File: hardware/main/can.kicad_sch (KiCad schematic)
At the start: 9 parts

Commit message: Schematics: finalize Analog Snubber and Supplies
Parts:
- C701: value ~ -> 50V 100nF X7R ±10% 0402
- C702: value ~ -> 50V 4.7n
- D701: renamed from D201; value ~ -> PESD1CAN
- R701: value ~ -> 4k7
- R702: value ~ -> 300R
- R703, R704: value ~ -> 520R
- R705: renamed from R202; value ~ -> NC
- renumbered U201 to U701
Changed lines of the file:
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@@
   (symbol (lib_id "power:GND") (at 133.35 101.6 0) (unit 1)
     (in_bom yes) (on_board yes)
-    (property "Reference" "#PWR0184" (id 0) (at 133.35 107.95 0)
+    (property "Reference" "#PWR0702" (id 0) (at 133.35 107.95 0)
       (effects (font (size 1.27 1.27)) hide)
     )
@@
       (effects (font (size 1.27 1.27)) (justify left))
     )
-    (property "Value" "~" (id 1) (at 117.0686 98.933 0)
+    (property "Value" "4k7" (id 1) (at 117.0686 98.933 0)
       (effects (font (size 1.27 1.27)) (justify left))
     )
@@
   (symbol (lib_id "power:GND") (at 118.11 76.2 0) (unit 1)
     (in_bom yes) (on_board yes)
-    (property "Reference" "#PWR0183" (id 0) (at 118.11 82.55 0)
+    (property "Reference" "#PWR0701" (id 0) (at 118.11 82.55 0)
       (effects (font (size 1.27 1.27)) hide)
     )
@@
     (in_bom yes) (on_board yes)
     (property "Reference" "C701" (id 0) (at 125.73 70.3834 90))
-    (property "Value" "~" (id 1) (at 125.73 72.6948 90))
+    (property "Value" "50V 100nF X7R ±10% 0402" (id 1) (at 125.73 72.6948 90))
     (property "Footprint" "" (id 2) (at 125.73 76.2 0)
       (effects (font (size 1.27 1.27)) hide)
     )
-    (property "Datasheet" "~" (id 3) (at 125.73 76.2 0)
+    (property "Datasheet" "https://lcsc.com/product-detail/Multilayer-Ceramic-Capacitors-MLCC-SMD-SMT_Murata-Electronics-GRM155R71H104KE14D_C77020.html" (id 3) (at 125.73 76.2 0)
       (effects (font (size 1.27 1.27)) hide)
     )
@@
   (symbol (lib_id "Interface_CAN_LIN:MCP2561-E-SN") (at 133.35 87.63 0) (unit 1)
     (in_bom yes) (on_board yes)
-    (property "Reference" "U201" (id 0) (at 133.35 72.8726 0))
+    (property "Reference" "U701" (id 0) (at 133.35 72.8726 0))
     (property "Value" "~" (id 1) (at 133.35 75.184 0))
     (property "Footprint" "" (id 2) (at 133.35 100.33 0)
@@
   (symbol (lib_id "Controle-rescue:D_TVS_x2_AAC-Device") (at 179.07 110.49 0) (unit 1)
     (in_bom yes) (on_board yes)
-    (property "Reference" "D201" (id 0) (at 179.07 104.9782 0))
-    (property "Value" "~" (id 1) (at 179.07 107.2896 0))
+    (property "Reference" "D701" (id 0) (at 179.07 104.9782 0))
+    (property "Value" "PESD1CAN" (id 1) (at 179.07 107.2896 0))
     (property "Footprint" "" (id 2) (at 179.07 110.49 0)
       (effects (font (size 1.27 1.27)) hide)
@@
   (symbol (lib_id "Device:R_Small") (at 179.07 102.87 270) (unit 1)
     (in_bom yes) (on_board yes)
-    (property "Reference" "R202" (id 0) (at 179.07 97.8916 90))
-    (property "Value" "~" (id 1) (at 179.07 100.203 90))
+    (property "Reference" "R705" (id 0) (at 179.07 97.8916 90))
+    (property "Value" "NC" (id 1) (at 179.07 100.203 90))
     (property "Footprint" "" (id 2) (at 179.07 102.87 0)
       (effects (font (size 1.27 1.27)) hide)
@@
   (symbol (lib_id "power:GND") (at 179.07 116.84 0) (unit 1)
     (in_bom yes) (on_board yes)
-    (property "Reference" "#PWR0182" (id 0) (at 179.07 123.19 0)
+    (property "Reference" "#PWR0704" (id 0) (at 179.07 123.19 0)
       (effects (font (size 1.27 1.27)) hide)
     )
@@
       (effects (font (size 1.27 1.27)) (justify left))
     )
-    (property "Value" "~" (id 1) (at 151.257 89.1286 0)
+    (property "Value" "300R" (id 1) (at 151.257 89.1286 0)
       (effects (font (size 1.27 1.27)) (justify left))
     )
@@
       (effects (font (size 1.27 1.27)) (justify left))
     )
-    (property "Value" "~" (id 1) (at 158.9786 81.407 0)
+    (property "Value" "520R" (id 1) (at 158.9786 81.407 0)
       (effects (font (size 1.27 1.27)) (justify left))
     )
@@
       (effects (font (size 1.27 1.27)) (justify left))
     )
-    (property "Value" "~" (id 1) (at 158.9786 91.567 0)
+    (property "Value" "520R" (id 1) (at 158.9786 91.567 0)
       (effects (font (size 1.27 1.27)) (justify left))
     )
@@
     (in_bom yes) (on_board yes)
     (property "Reference" "C702" (id 0) (at 167.64 81.8134 90))
-    (property "Value" "~" (id 1) (at 167.64 84.1248 90))
+    (property "Value" "50V 4.7n " (id 1) (at 167.64 84.1248 90))
     (property "Footprint" "" (id 2) (at 167.64 87.63 0)
       (effects (font (size 1.27 1.27)) hide)
@@
   (symbol (lib_id "power:GND") (at 175.26 88.9 0) (unit 1)
     (in_bom yes) (on_board yes)
-    (property "Reference" "#PWR0181" (id 0) (at 175.26 95.25 0)
+    (property "Reference" "#PWR0703" (id 0) (at 175.26 95.25 0)
       (effects (font (size 1.27 1.27)) hide)
     )

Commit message: Schematics: Modified component values
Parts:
- C702: value 50V 4.7n -> 50V 4.7nF X7R ±5% 0603
- R701: value 4k7 -> 4k7 0805
- R702: value 300R -> 300R 0805
- R703, R704: value 520R -> 520R 0805
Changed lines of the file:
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@@
       (effects (font (size 1.27 1.27)) (justify left))
     )
-    (property "Value" "4k7" (id 1) (at 117.0686 98.933 0)
+    (property "Value" "4k7 0805" (id 1) (at 117.0686 98.933 0)
       (effects (font (size 1.27 1.27)) (justify left))
     )
@@
       (effects (font (size 1.27 1.27)) (justify left))
     )
-    (property "Value" "300R" (id 1) (at 151.257 89.1286 0)
+    (property "Value" "300R 0805" (id 1) (at 151.257 89.1286 0)
       (effects (font (size 1.27 1.27)) (justify left))
     )
@@
       (effects (font (size 1.27 1.27)) (justify left))
     )
-    (property "Value" "520R" (id 1) (at 158.9786 81.407 0)
+    (property "Value" "520R 0805" (id 1) (at 158.9786 81.407 0)
       (effects (font (size 1.27 1.27)) (justify left))
     )
@@
       (effects (font (size 1.27 1.27)) (justify left))
     )
-    (property "Value" "520R" (id 1) (at 158.9786 91.567 0)
+    (property "Value" "520R 0805" (id 1) (at 158.9786 91.567 0)
       (effects (font (size 1.27 1.27)) (justify left))
     )
@@
     (in_bom yes) (on_board yes)
     (property "Reference" "C702" (id 0) (at 167.64 81.8134 90))
-    (property "Value" "50V 4.7n " (id 1) (at 167.64 84.1248 90))
+    (property "Value" "50V 4.7nF X7R ±5% 0603" (id 1) (at 167.64 84.1248 90))
     (property "Footprint" "" (id 2) (at 167.64 87.63 0)
       (effects (font (size 1.27 1.27)) hide)

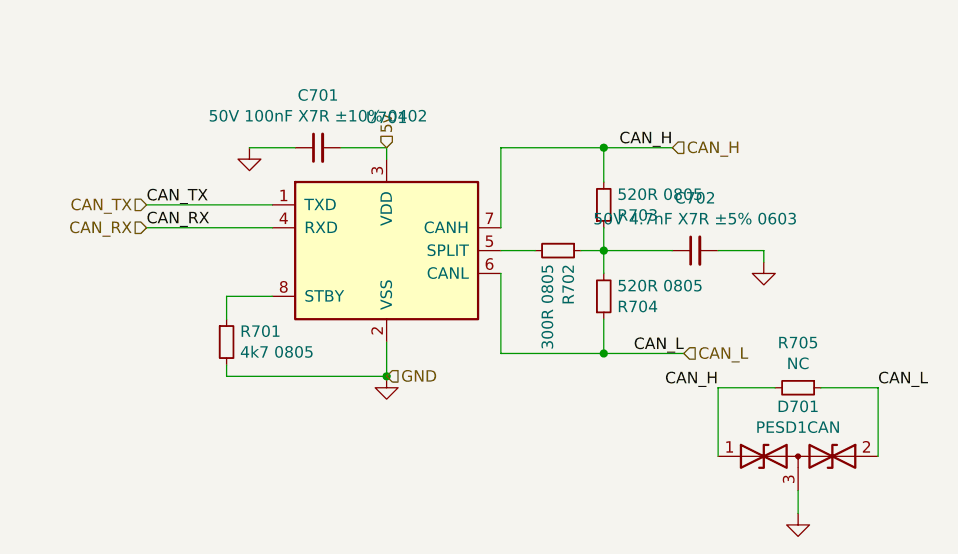
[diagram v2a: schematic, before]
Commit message: Schematics: Run DRC and fix errors and some warnings, also added Zenite kicad library repo as submodule
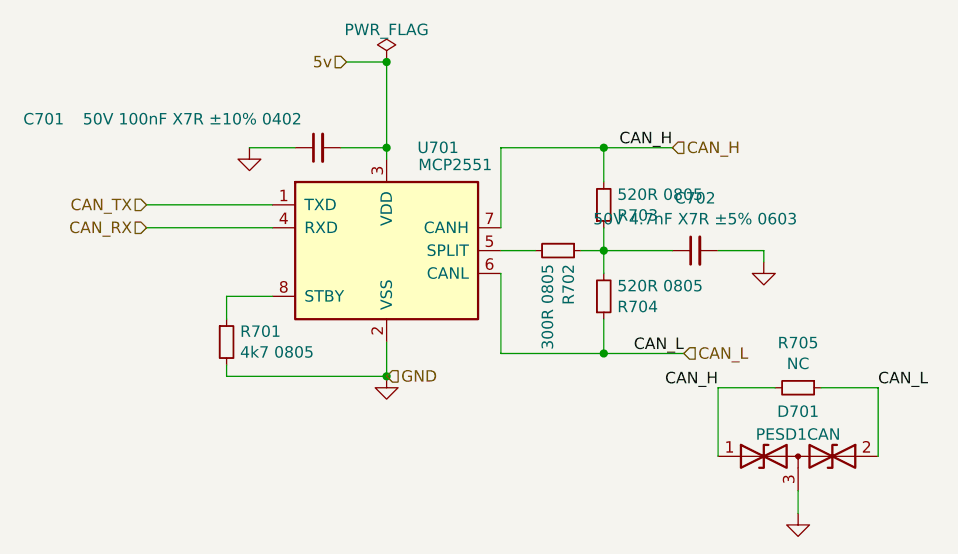
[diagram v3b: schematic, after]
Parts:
- removed D701: PESD1CAN, symbol Controle-rescue:D_TVS_x2_AAC-Device
- added D701: PESD1CAN, Package_TO_SOT_SMD:SOT-23_Handsoldering, symbol Device:D_TVS_Dual_AAC
- C701: footprint (none) -> Capacitor_SMD:C_0402_1005Metric_Pad0.74x0.62mm_HandSolder
- C702: footprint (none) -> Capacitor_SMD:C_0603_1608Metric_Pad1.08x0.95mm_HandSolder
- R701, R702, R703, R704, R705: footprint (none) -> Resistor_SMD:R_0805_2012Metric_Pad1.20x1.40mm_HandSolder
- U701: value ~ -> MCP2551; footprint (none) -> Package_SO:SOIC-8_3.9x4.9mm_P1.27mm
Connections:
- net CAN_H: now also D701.1 (A1)
- net CAN_L: now also D701.2 (A2)
- net GND: now also D701.3 (common)
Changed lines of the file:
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@@
   (junction (at 133.35 101.6) (diameter 0) (color 0 0 0 0)
   )
+  (junction (at 133.35 66.675) (diameter 0) (color 0 0 0 0)
+  )
   (junction (at 157.48 87.63) (diameter 0) (color 0 0 0 0)
   )
+  (junction (at 133.35 76.2) (diameter 0) (color 0 0 0 0)
+  )
   (junction (at 157.48 76.2) (diameter 0) (color 0 0 0 0)
   )
@@
     (stroke (width 0) (type default) (color 0 0 0 0))
   )
+  (wire (pts (xy 128.905 66.675) (xy 133.35 66.675))
+    (stroke (width 0) (type default) (color 0 0 0 0))
+  )
   (wire (pts (xy 133.35 76.2) (xy 133.35 77.47))
     (stroke (width 0) (type default) (color 0 0 0 0))
@@
   )
   (wire (pts (xy 115.57 101.6) (xy 133.35 101.6))
+    (stroke (width 0) (type default) (color 0 0 0 0))
+  )
+  (wire (pts (xy 133.35 66.675) (xy 133.35 76.2))
     (stroke (width 0) (type default) (color 0 0 0 0))
   )
@@
     (effects (font (size 1.27 1.27)) (justify right bottom))
   )
-  (label "CAN_TX" (at 106.68 82.55 0)
-    (effects (font (size 1.27 1.27)) (justify left bottom))
-  )
   (label "CAN_H" (at 170.18 102.87 180)
     (effects (font (size 1.27 1.27)) (justify right bottom))
   )
-  (label "CAN_RX" (at 106.68 85.09 0)
-    (effects (font (size 1.27 1.27)) (justify left bottom))
-  )
   (hierarchical_label "CAN_TX" (shape input) (at 106.68 82.55 180)
     (effects (font (size 1.27 1.27)) (justify right))
@@
     (effects (font (size 1.27 1.27)) (justify left))
   )
-  (hierarchical_label "5v" (shape input) (at 133.35 76.2 90)
-    (effects (font (size 1.27 1.27)) (justify left))
+  (hierarchical_label "5v" (shape input) (at 128.905 66.675 180)
+    (effects (font (size 1.27 1.27)) (justify right))
   )
   (hierarchical_label "CAN_L" (shape input) (at 166.37 99.06 0)
@@
       (effects (font (size 1.27 1.27)) (justify left))
     )
-    (property "Footprint" "" (id 2) (at 115.57 97.79 0)
+    (property "Footprint" "Resistor_SMD:R_0805_2012Metric_Pad1.20x1.40mm_HandSolder" (id 2) (at 115.57 97.79 0)
       (effects (font (size 1.27 1.27)) hide)
     )
@@
   (symbol (lib_id "Device:C_Small") (at 125.73 76.2 90) (unit 1)
     (in_bom yes) (on_board yes)
-    (property "Reference" "C701" (id 0) (at 125.73 70.3834 90))
-    (property "Value" "50V 100nF X7R ±10% 0402" (id 1) (at 125.73 72.6948 90))
-    (property "Footprint" "" (id 2) (at 125.73 76.2 0)
+    (property "Reference" "C701" (id 0) (at 95.25 73.025 90))
+    (property "Value" "50V 100nF X7R ±10% 0402" (id 1) (at 111.76 73.025 90))
+    (property "Footprint" "Capacitor_SMD:C_0402_1005Metric_Pad0.74x0.62mm_HandSolder" (id 2) (at 125.73 76.2 0)
       (effects (font (size 1.27 1.27)) hide)
     )
@@
   (symbol (lib_id "Interface_CAN_LIN:MCP2561-E-SN") (at 133.35 87.63 0) (unit 1)
     (in_bom yes) (on_board yes)
-    (property "Reference" "U701" (id 0) (at 133.35 72.8726 0))
-    (property "Value" "~" (id 1) (at 133.35 75.184 0))
-    (property "Footprint" "" (id 2) (at 133.35 100.33 0)
+    (property "Reference" "U701" (id 0) (at 139.065 76.2 0))
+    (property "Value" "MCP2551" (id 1) (at 140.97 78.105 0))
+    (property "Footprint" "Package_SO:SOIC-8_3.9x4.9mm_P1.27mm" (id 2) (at 133.35 100.33 0)
       (effects (font (size 1.27 1.27) italic) hide)
     )
@@
     (pin "8")
   )
-  (symbol (lib_id "Controle-rescue:D_TVS_x2_AAC-Device") (at 179.07 110.49 0) (unit 1)
-    (in_bom yes) (on_board yes)
-    (property "Reference" "D701" (id 0) (at 179.07 104.9782 0))
-    (property "Value" "PESD1CAN" (id 1) (at 179.07 107.2896 0))
-    (property "Footprint" "" (id 2) (at 179.07 110.49 0)
-      (effects (font (size 1.27 1.27)) hide)
-    )
-    (property "Datasheet" "~" (id 3) (at 179.07 110.49 0)
-      (effects (font (size 1.27 1.27)) hide)
-    )
-    (pin "1")
-    (pin "2")
-    (pin "3")
-  )
   (symbol (lib_id "Device:R_Small") (at 179.07 102.87 270) (unit 1)
     (in_bom yes) (on_board yes)
     (property "Reference" "R705" (id 0) (at 179.07 97.8916 90))
     (property "Value" "NC" (id 1) (at 179.07 100.203 90))
-    (property "Footprint" "" (id 2) (at 179.07 102.87 0)
+    (property "Footprint" "Resistor_SMD:R_0805_2012Metric_Pad1.20x1.40mm_HandSolder" (id 2) (at 179.07 102.87 0)
       (effects (font (size 1.27 1.27)) hide)
     )
@@
       (effects (font (size 1.27 1.27)) (justify left))
     )
-    (property "Footprint" "" (id 2) (at 152.4 87.63 0)
+    (property "Footprint" "Resistor_SMD:R_0805_2012Metric_Pad1.20x1.40mm_HandSolder" (id 2) (at 152.4 87.63 0)
       (effects (font (size 1.27 1.27)) hide)
     )
@@
       (effects (font (size 1.27 1.27)) (justify left))
     )
-    (property "Footprint" "" (id 2) (at 157.48 82.55 0)
+    (property "Footprint" "Resistor_SMD:R_0805_2012Metric_Pad1.20x1.40mm_HandSolder" (id 2) (at 157.48 82.55 0)
       (effects (font (size 1.27 1.27)) hide)
     )
@@
       (effects (font (size 1.27 1.27)) (justify left))
     )
-    (property "Footprint" "" (id 2) (at 157.48 92.71 0)
+    (property "Footprint" "Resistor_SMD:R_0805_2012Metric_Pad1.20x1.40mm_HandSolder" (id 2) (at 157.48 92.71 0)
       (effects (font (size 1.27 1.27)) hide)
     )
@@
     (property "Reference" "C702" (id 0) (at 167.64 81.8134 90))
     (property "Value" "50V 4.7nF X7R ±5% 0603" (id 1) (at 167.64 84.1248 90))
-    (property "Footprint" "" (id 2) (at 167.64 87.63 0)
+    (property "Footprint" "Capacitor_SMD:C_0603_1608Metric_Pad1.08x0.95mm_HandSolder" (id 2) (at 167.64 87.63 0)
       (effects (font (size 1.27 1.27)) hide)
     )
@@
     (pin "1")
   )
+  (symbol (lib_id "power:PWR_FLAG") (at 133.35 66.675 0) (unit 1)
+    (in_bom yes) (on_board yes) (fields_autoplaced)
+    (property "Reference" "#FLG0701" (id 0) (at 133.35 64.77 0)
+      (effects (font (size 1.27 1.27)) hide)
+    )
+    (property "Value" "PWR_FLAG" (id 1) (at 133.35 63.0992 0))
+    (property "Footprint" "" (id 2) (at 133.35 66.675 0)
+      (effects (font (size 1.27 1.27)) hide)
+    )
+    (property "Datasheet" "~" (id 3) (at 133.35 66.675 0)
+      (effects (font (size 1.27 1.27)) hide)
+    )
+    (pin "1")
+  )
+  (symbol (lib_id "Device:D_TVS_Dual_AAC") (at 179.07 110.49 0) (unit 1)
+    (in_bom yes) (on_board yes) (fields_autoplaced)
+    (property "Reference" "D701" (id 0) (at 179.07 105.5202 0))
+    (property "Value" "PESD1CAN" (id 1) (at 179.07 108.0571 0))
+    (property "Footprint" "Package_TO_SOT_SMD:SOT-23_Handsoldering" (id 2) (at 175.26 110.49 0)
+      (effects (font (size 1.27 1.27)) hide)
+    )
+    (property "Datasheet" "~" (id 3) (at 175.26 110.49 0)
+      (effects (font (size 1.27 1.27)) hide)
+    )
+    (pin "1")
+    (pin "2")
+    (pin "3")
+  )
 )

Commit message: Layout: Finalize first vesion of control (DRC ok) and modify vias for better via density
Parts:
- U701: value MCP2551 -> MCP2561
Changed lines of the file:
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@@
     (in_bom yes) (on_board yes)
     (property "Reference" "U701" (id 0) (at 139.065 76.2 0))
-    (property "Value" "MCP2551" (id 1) (at 140.97 78.105 0))
+    (property "Value" "MCP2561" (id 1) (at 140.97 78.105 0))
     (property "Footprint" "Package_SO:SOIC-8_3.9x4.9mm_P1.27mm" (id 2) (at 133.35 100.33 0)
       (effects (font (size 1.27 1.27) italic) hide)
